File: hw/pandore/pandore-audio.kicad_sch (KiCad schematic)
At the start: 0 parts

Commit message: added usb, hdmi and combo xlrtrs connectors resized pcb for something realistic (still wip)
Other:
- added sheet Audio inputs (pandore-audio-inputs.kicad_sch)
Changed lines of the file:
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@@
 		(company "${corp}")
 	)
+	(sheet
+		(at 35.56 29.21)
+		(size 43.18 19.05)
+		(exclude_from_sim no)
+		(in_bom yes)
+		(on_board yes)
+		(dnp no)
+		(stroke
+			(width 0.1524)
+			(type solid)
+		)
+		(fill
+			(color 0 0 0 0.0000)
+		)
+		(property "Sheetname" "Audio inputs"
+			(at 56.515 33.02 0)
+			(do_not_autoplace yes)
+			(effects
+				(font
+					(size 3 3)
+					(thickness 0.6)
+					(bold yes)
+				)
+			)
+		)
+		(property "Sheetfile" "pandore-audio-inputs.kicad_sch"
+			(at 36.068 66.802 0)
+			(effects
+				(font
+					(size 1.27 1.27)
+				)
+				(justify left bottom)
+				(hide yes)
+			)
+		)
+		(property "pageNb" "Page ${#}"
+			(at 56.515 36.83 0)
+			(effects
+				(font
+					(size 1.27 1.27)
+					(thickness 0.1588)
+				)
+			)
+		)
+		(instances
+			(project "pandore"
+				(path "/e55f2700-f75a-4062-8a27-fe258faa8966/b4e2772d-7748-46ec-bd38-bc8e72cebcb8"
+					(page "20")
+				)
+			)
+		)
+	)
 )

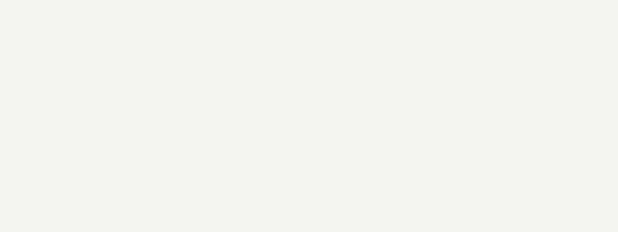
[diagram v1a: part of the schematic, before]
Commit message: added all remaining connectors (only missing M.2 now)
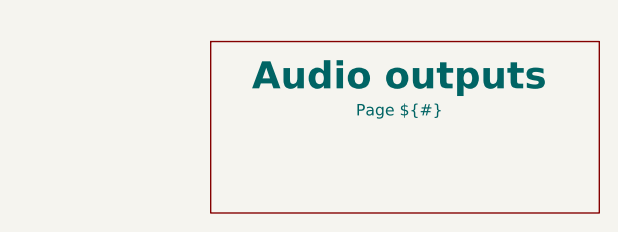
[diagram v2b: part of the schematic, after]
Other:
- added sheet Audio outputs (pandore-audio-outputs.kicad_sch)
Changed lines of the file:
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@@
+		)
+	)
+	(sheet
+		(at 199.39 31.75)
+		(size 43.18 19.05)
+		(exclude_from_sim no)
+		(in_bom yes)
+		(on_board yes)
+		(dnp no)
+		(stroke
+			(width 0.1524)
+			(type solid)
+		)
+		(fill
+			(color 0 0 0 0.0000)
+		)
+		(property "Sheetname" "Audio outputs"
+			(at 220.345 35.56 0)
+			(do_not_autoplace yes)
+			(effects
+				(font
+					(size 3 3)
+					(thickness 0.6)
+					(bold yes)
+				)
+			)
+		)
+		(property "Sheetfile" "pandore-audio-outputs.kicad_sch"
+			(at 199.898 69.342 0)
+			(effects
+				(font
+					(size 1.27 1.27)
+				)
+				(justify left bottom)
+				(hide yes)
+			)
+		)
+		(property "pageNb" "Page ${#}"
+			(at 220.345 39.37 0)
+			(effects
+				(font
+					(size 1.27 1.27)
+					(thickness 0.1588)
+				)
+			)
+		)
+		(instances
+			(project "pandore"
+				(path "/e55f2700-f75a-4062-8a27-fe258faa8966/b4e2772d-7748-46ec-bd38-bc8e72cebcb8"
+					(page "21")
+				)
+			)
 		)
 	)

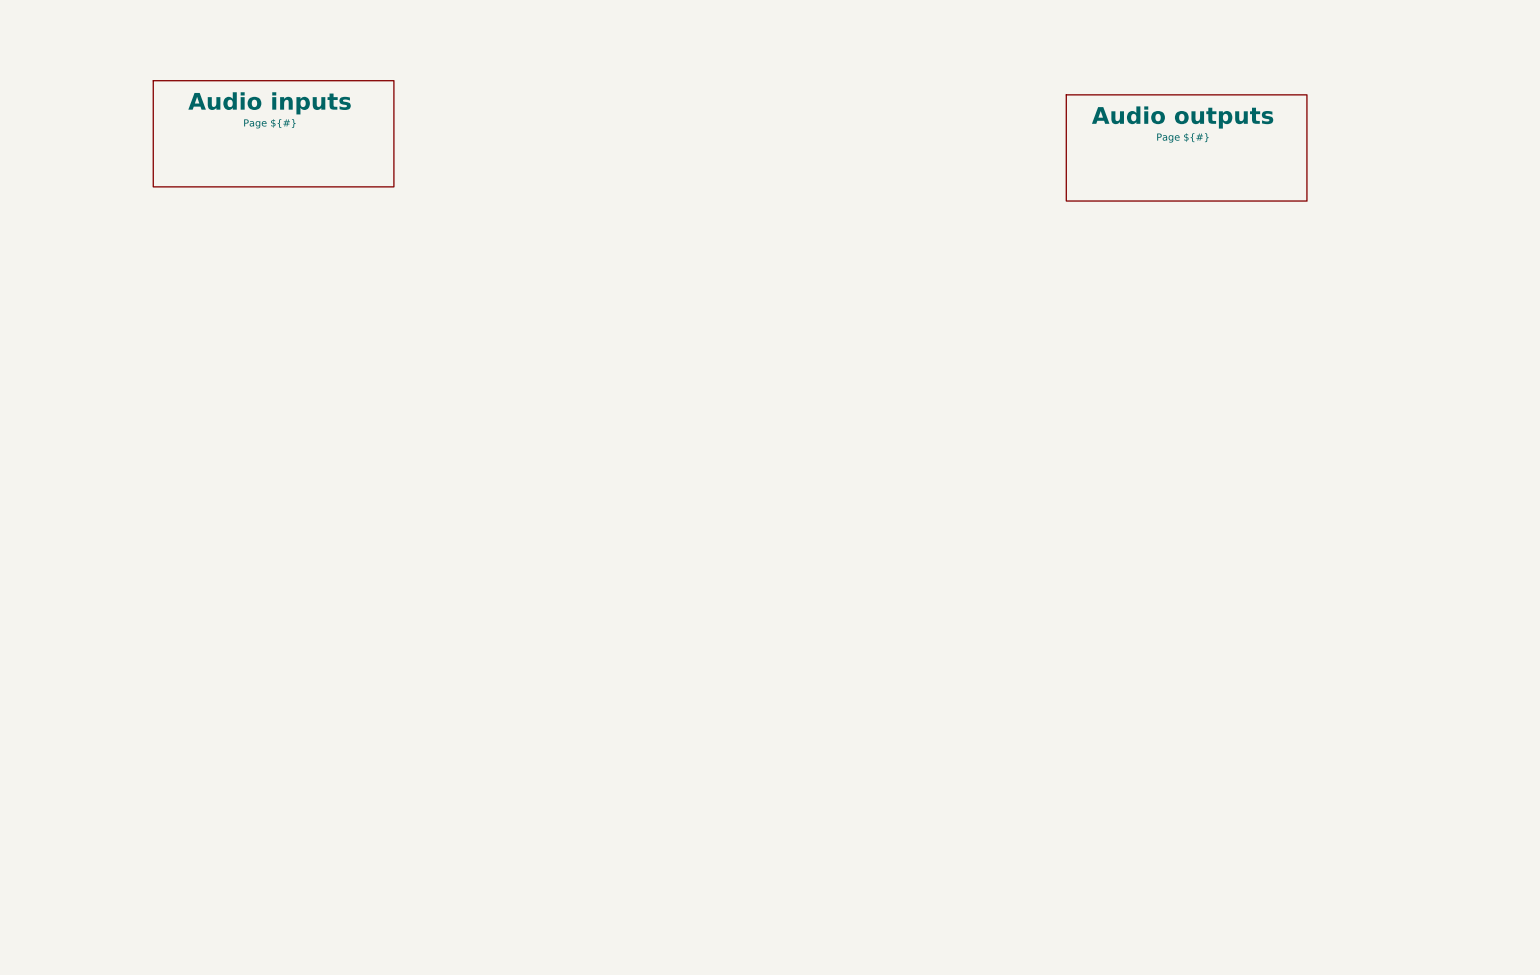
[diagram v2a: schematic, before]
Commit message: Added lots to sch and pcb: eth passive, audio codec, midi, teensy Corrected and added support for M.2
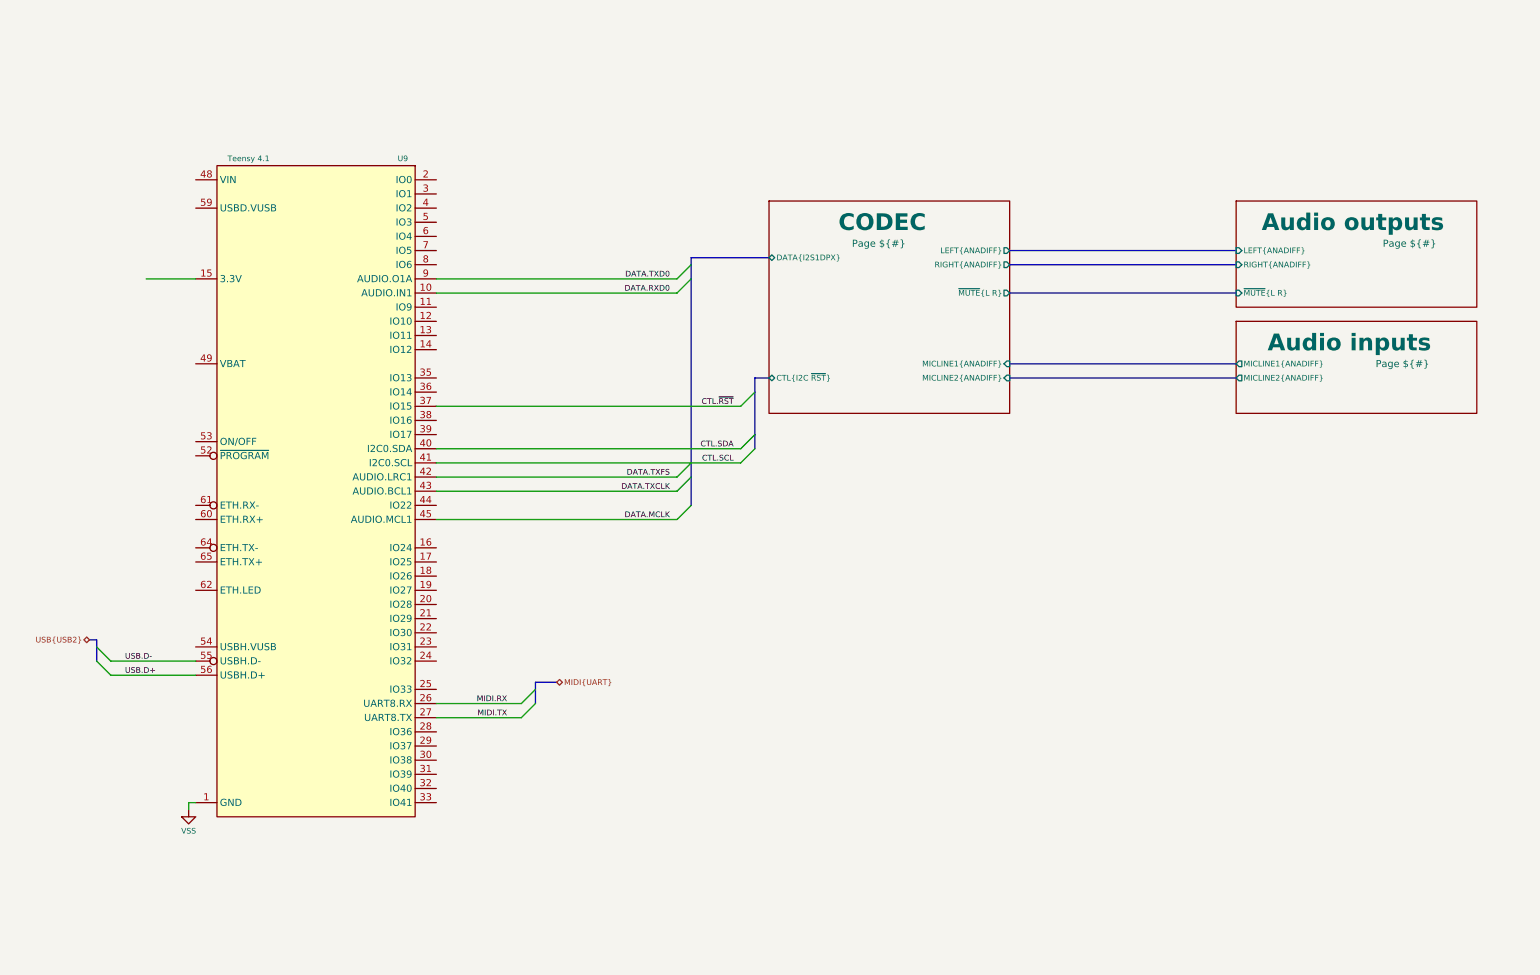
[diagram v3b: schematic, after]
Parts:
- added U9: Teensy 4.1, reekilib_som:teensy_4.1, symbol reekilib_som:Teensy-4.1
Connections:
- new net: U9.15 (3.3V), U9.46 (3.3V), U9.50 (3.3V)
- new net CTL.SCL: U9.41 (IO19)
- new net CTL.SDA: U9.40 (IO18)
- new net CTL.~{RST}: U9.37 (IO15)
- new net DATA.MCLK: U9.45 (IO23)
- new net DATA.RXD0: U9.10 (IO8)
- new net DATA.TXCLK: U9.43 (IO21)
- new net DATA.TXD0: U9.9 (IO7)
- new net DATA.TXFS: U9.42 (IO20)
- new net MIDI.RX: U9.26 (IO34)
- new net MIDI.TX: U9.27 (IO35)
- new net USB.D+: U9.56 (USBH.D+)
- new net USB.D-: U9.55 (USBH.D-)
- new net VSS: U9.1 (GND), U9.34 (GND), U9.47 (GND), U9.51 (GND), U9.57 (GND), U9.58 (GND), U9.63 (GND)
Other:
- added sheet CODEC (pandore-audio-codec.kicad_sch)
- sheet Audio inputs ports: added MICLINE1{ANADIFF}, MICLINE2{ANADIFF}; removed none
- sheet Audio outputs ports: added LEFT{ANADIFF}, RIGHT{ANADIFF}, ~{MUTE}{L R}; removed none

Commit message: lots of work done all around
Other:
- added sheet Power (pandore-audio-power.kicad_sch)
- sheet Audio inputs ports: added VCM, ~{MUTE}{L R}; removed none
- sheet Audio outputs ports: added VCM; removed none
- sheet CODEC ports: added VCM; removed none

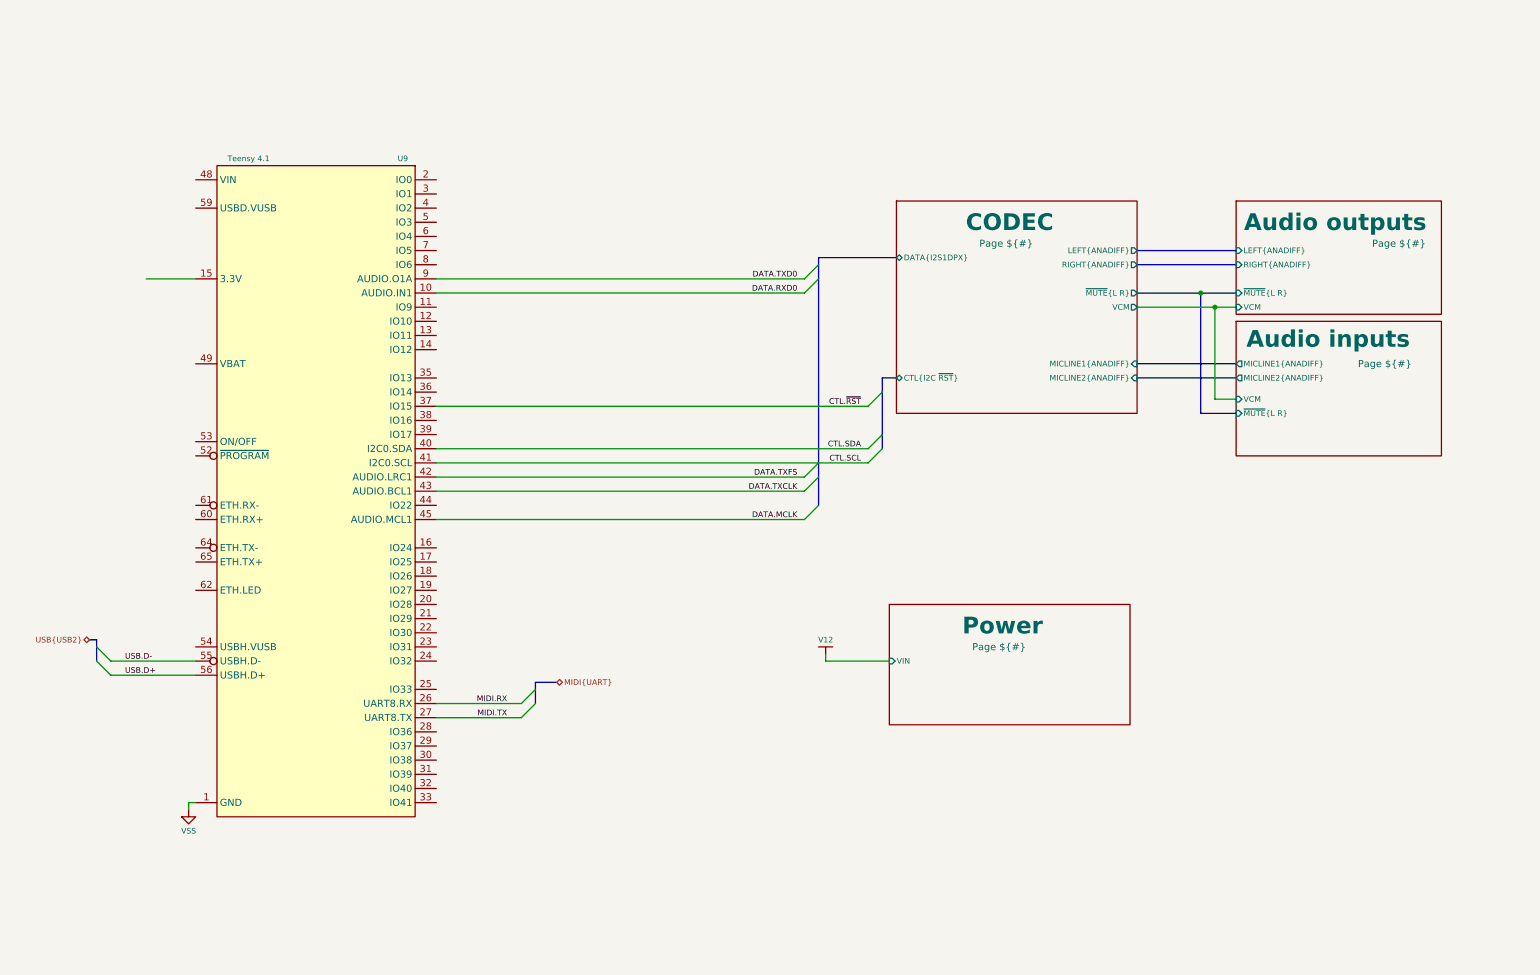
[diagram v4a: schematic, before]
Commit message: added power stuff revised M.2 for higher model and added m.2 mounts added power tap terminals
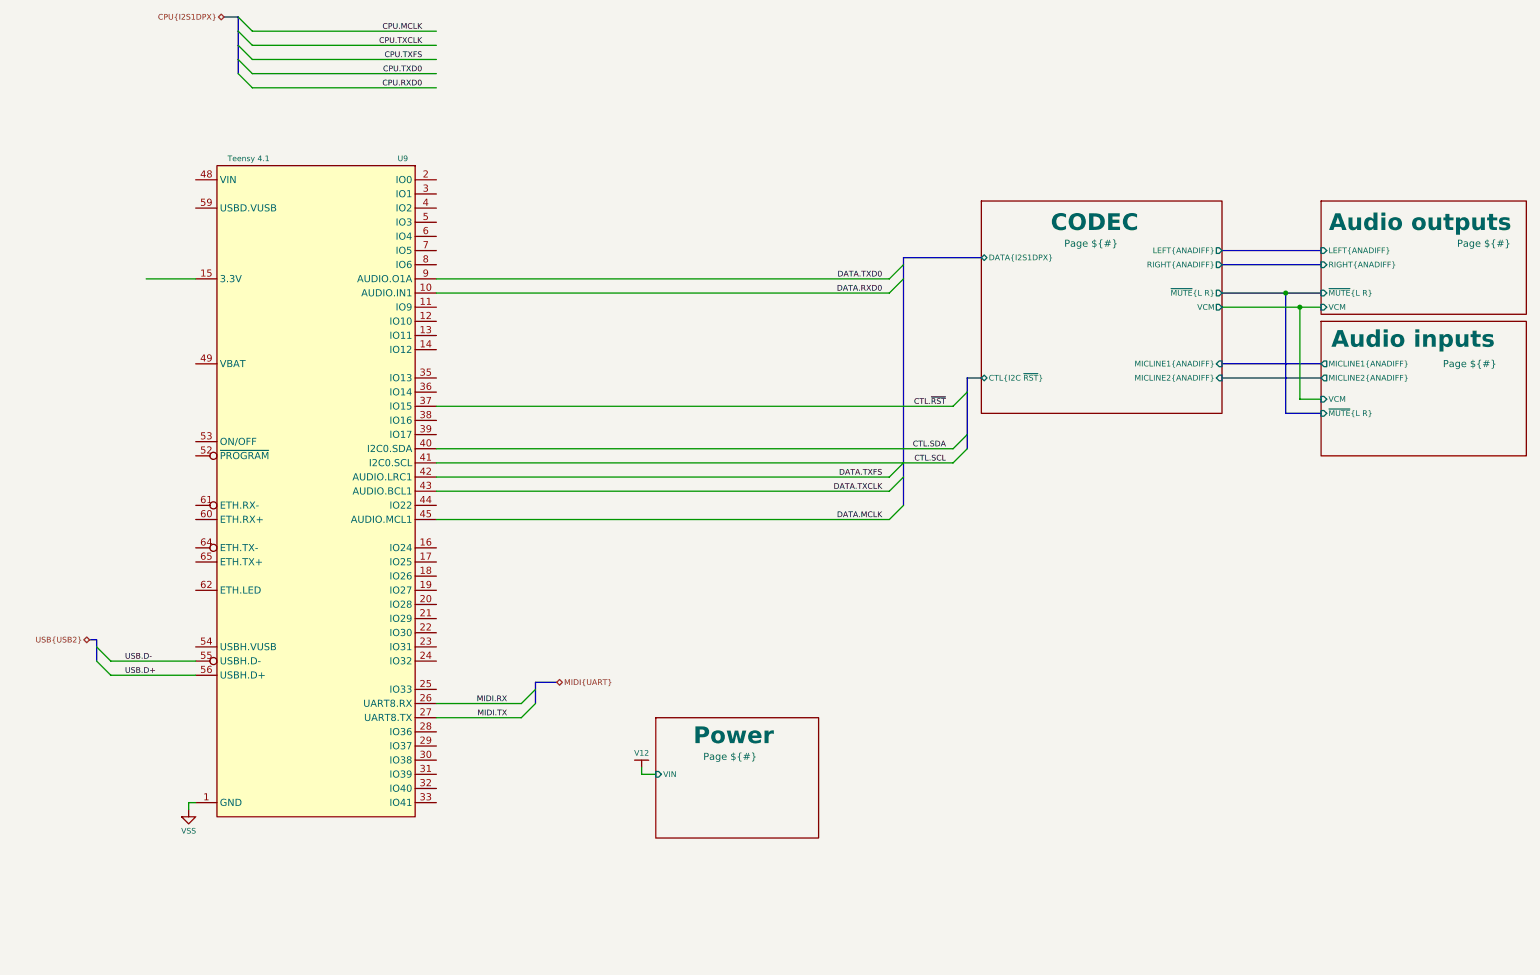
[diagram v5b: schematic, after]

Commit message: added i2s/i2c isolation for audio section
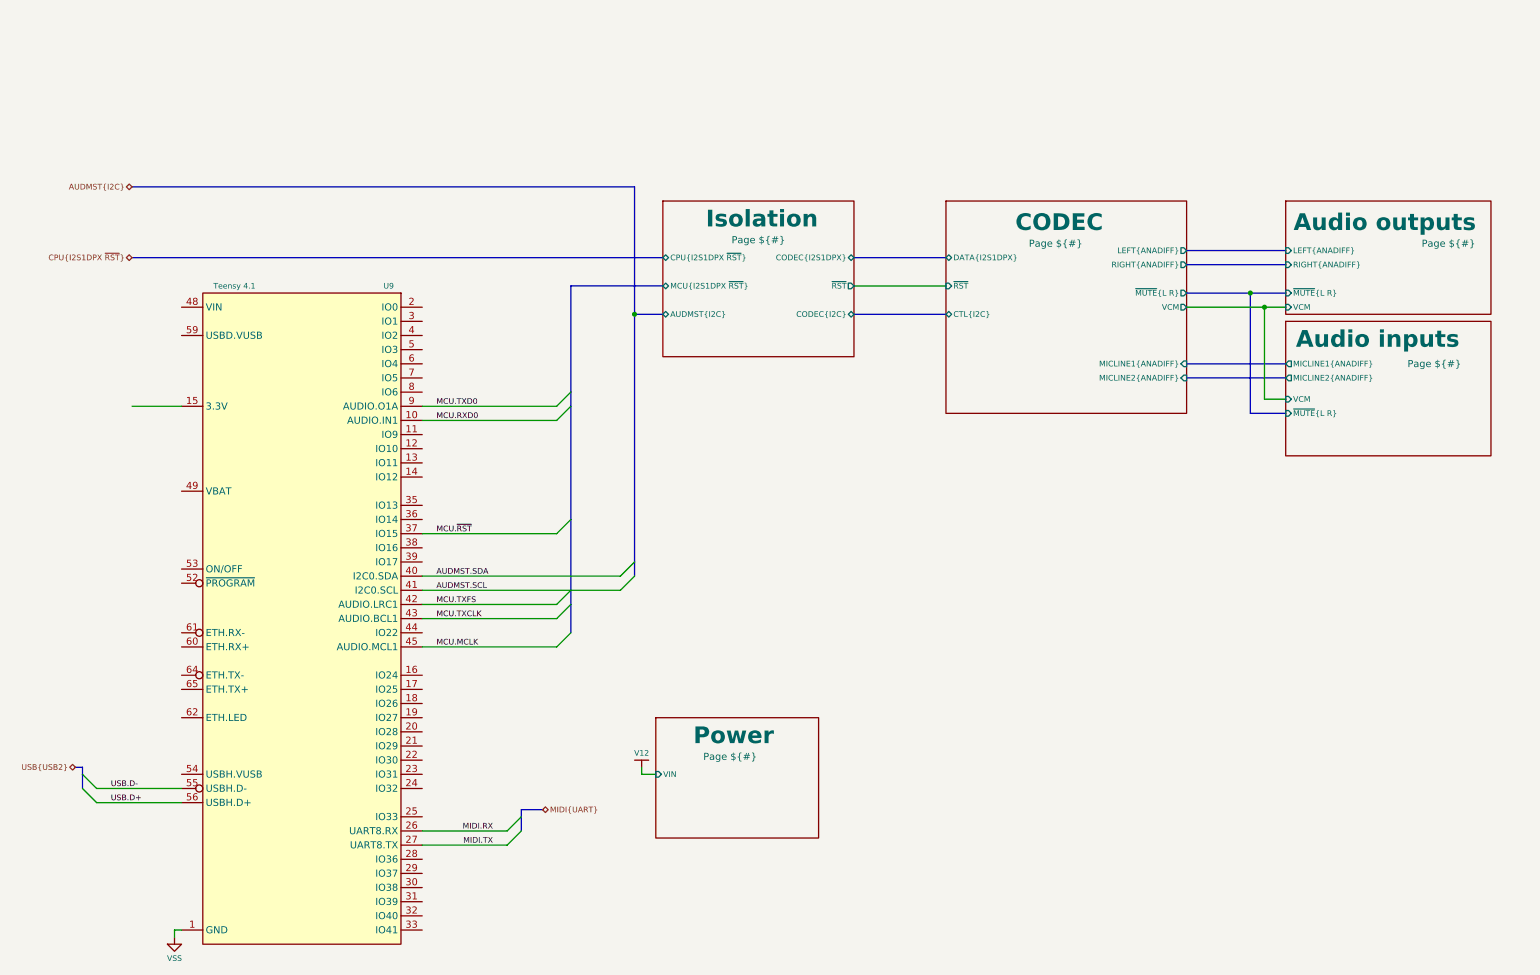
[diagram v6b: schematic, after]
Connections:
- net CTL.SCL renamed AUDMST.SCL
- net CTL.SDA renamed AUDMST.SDA
- net CTL.~{RST} renamed MCU.~{RST}
- net DATA.MCLK renamed MCU.MCLK
- net DATA.RXD0 renamed MCU.RXD0
- net DATA.TXCLK renamed MCU.TXCLK
- net DATA.TXD0 renamed MCU.TXD0
- net DATA.TXFS renamed MCU.TXFS
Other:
- added sheet Isolation (pandore-audio-isolation.kicad_sch)
- sheet CODEC ports: added CTL{I2C}, ~{RST}; removed CTL{I2C ~{RST}}
- moved on the sheet: U9
